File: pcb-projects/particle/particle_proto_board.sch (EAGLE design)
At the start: 5 parts, among them IC1 ATTINY20-SOIC-14S1, IC2 DMC2400UV-SOT563, IC3 DMC2400UV-SOT563

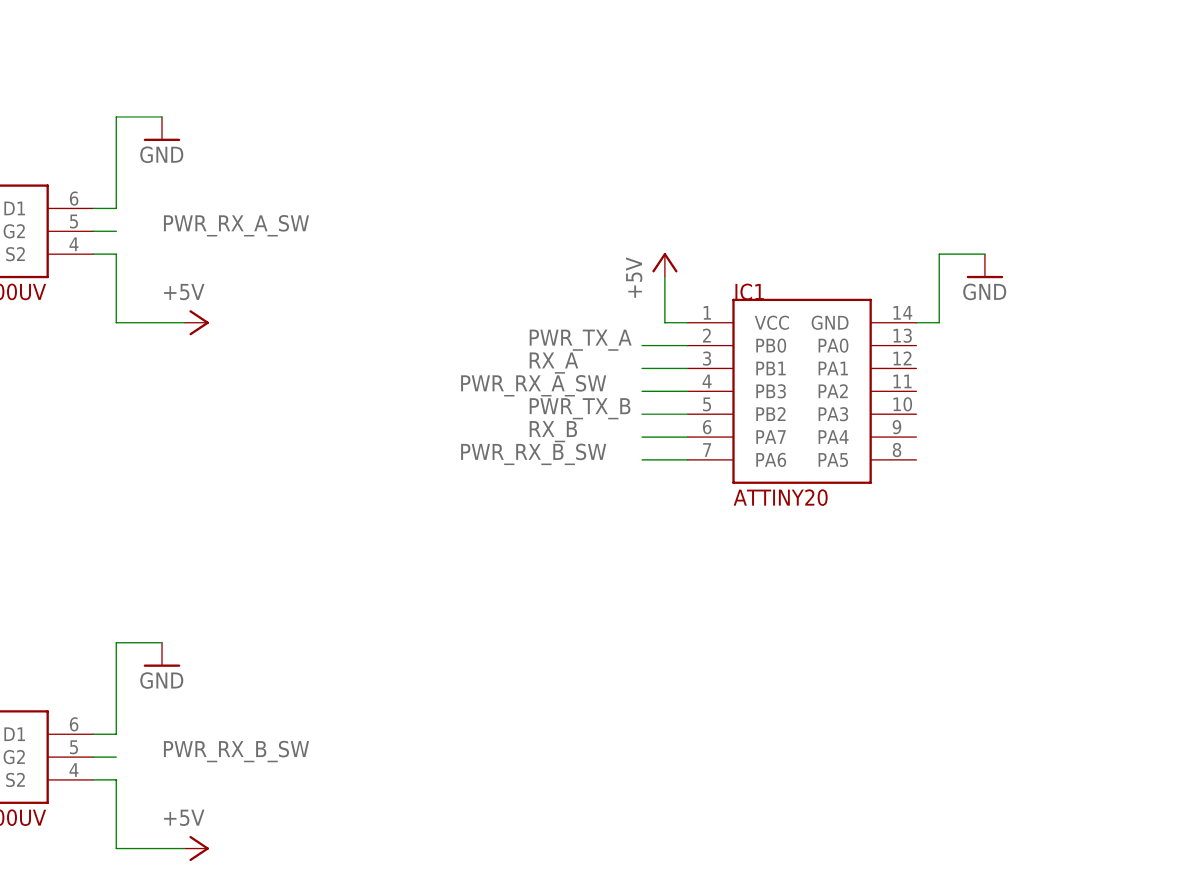
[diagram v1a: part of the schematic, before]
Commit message: begun with tpi connector
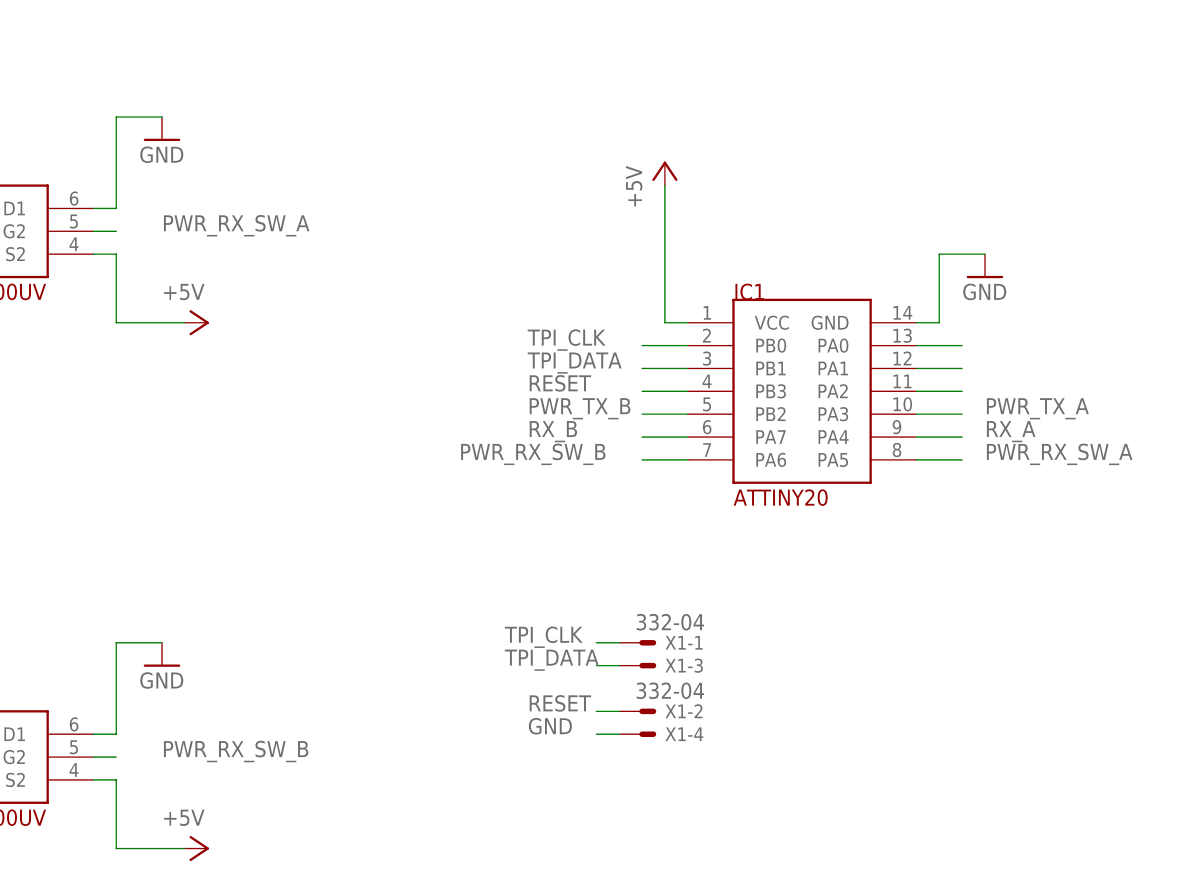
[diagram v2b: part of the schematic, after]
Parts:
- added X1: 332-04, con-garry:332-04
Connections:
- net PWR_RX_B_SW renamed PWR_RX_SW_B
- removed net PWR_RX_A_SW: IC1.PB3, IC2.G2
- new net N$4: IC1.PA2
- new net N$5: IC1.PA1
- new net N$6: IC1.PA0
- new net PWR_RX_SW_A: IC1.PA5, IC2.G2
- new net RESET: IC1.PB3, X1-2.S
- new net TPI_CLK: IC1.PB0, X1-1.S
- new net TPI_DATA: IC1.PB1, X1-3.S
- net GND: now also X1-4.S
- net PWR_TX_A: now also IC1.PA3; no longer IC1.PB0
- net RX_A: now also IC1.PA4; no longer IC1.PB1
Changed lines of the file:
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@@
 <?xml version="1.0" encoding="utf-8"?>
 <!DOCTYPE eagle SYSTEM "eagle.dtd">
-<eagle version="6.6.0">
+<eagle version="7.2.0">
 <drawing>
 <settings>
@@
 <part name="R1" library="rcl" deviceset="R-EU_" device="R1206" value="1k"/>
 <part name="R2" library="rcl" deviceset="R-EU_" device="R1206" value="1k"/>
+<part name="X1" library="con-garry" deviceset="332-04" device=""/>
 </parts>
 <sheets>
@@
 <instance part="IC1" gate="G$1" x="91.44" y="83.82"/>
 <instance part="IC2" gate="G$1" x="0" y="101.6"/>
-<instance part="P+2" gate="1" x="76.2" y="99.06"/>
+<instance part="P+2" gate="1" x="76.2" y="109.22"/>
 <instance part="GND1" gate="1" x="111.76" y="96.52"/>
 <instance part="GND2" gate="1" x="20.32" y="111.76"/>
@@
 <instance part="R1" gate="G$1" x="-22.86" y="114.3" rot="R90"/>
 <instance part="R2" gate="G$1" x="-22.86" y="55.88" rot="R90"/>
+<instance part="X1" gate="-1" x="73.66" y="55.88"/>
+<instance part="X1" gate="-2" x="73.66" y="48.26"/>
+<instance part="X1" gate="-3" x="73.66" y="53.34"/>
+<instance part="X1" gate="-4" x="73.66" y="45.72"/>
 </instances>
 <busses>
@@
 <pinref part="IC1" gate="G$1" pin="VCC"/>
 <wire x1="78.74" y1="91.44" x2="76.2" y2="91.44" width="0.1524" layer="91"/>
-<wire x1="76.2" y1="91.44" x2="76.2" y2="96.52" width="0.1524" layer="91"/>
+<wire x1="76.2" y1="91.44" x2="76.2" y2="106.68" width="0.1524" layer="91"/>
 <pinref part="P+2" gate="1" pin="+5V"/>
 </segment>
@@
 <wire x1="15.24" y1="55.88" x2="20.32" y2="55.88" width="0.1524" layer="91"/>
 </segment>
-</net>
-<net name="PWR_TX_A" class="0">
+<segment>
+<pinref part="X1" gate="-4" pin="S"/>
+<wire x1="71.12" y1="45.72" x2="68.58" y2="45.72" width="0.1524" layer="91"/>
+<label x="60.96" y="45.72" size="1.778" layer="95"/>
+</segment>
+</net>
+<net name="TPI_CLK" class="0">
 <segment>
 <pinref part="IC1" gate="G$1" pin="PB0"/>
@@
 </segment>
 <segment>
-<pinref part="IC2" gate="G$1" pin="G1"/>
-<wire x1="-12.7" y1="101.6" x2="-15.24" y2="101.6" width="0.1524" layer="91"/>
-<label x="-30.48" y="101.6" size="1.778" layer="95"/>
+<pinref part="X1" gate="-1" pin="S"/>
+<wire x1="71.12" y1="55.88" x2="68.58" y2="55.88" width="0.1524" layer="91"/>
+<label x="58.42" y="55.88" size="1.778" layer="95"/>
 </segment>
 </net>
@@
 </segment>
 </net>
-<net name="RX_A" class="0">
+<net name="TPI_DATA" class="0">
 <segment>
 <pinref part="IC1" gate="G$1" pin="PB1"/>
@@
 </segment>
 <segment>
-<pinref part="IC2" gate="G$1" pin="D2"/>
-<wire x1="-12.7" y1="99.06" x2="-15.24" y2="99.06" width="0.1524" layer="91"/>
-<label x="-30.48" y="99.06" size="1.778" layer="95"/>
-</segment>
-</net>
-<net name="PWR_RX_A_SW" class="0">
+<pinref part="X1" gate="-3" pin="S"/>
+<wire x1="71.12" y1="53.34" x2="68.58" y2="53.34" width="0.1524" layer="91"/>
+<label x="58.42" y="53.34" size="1.778" layer="95"/>
+</segment>
+</net>
+<net name="RESET" class="0">
 <segment>
 <pinref part="IC1" gate="G$1" pin="PB3"/>
 <wire x1="78.74" y1="83.82" x2="73.66" y2="83.82" width="0.1524" layer="91"/>
-<label x="53.34" y="83.82" size="1.778" layer="95"/>
-</segment>
-<segment>
-<pinref part="IC2" gate="G$1" pin="G2"/>
-<wire x1="12.7" y1="101.6" x2="15.24" y2="101.6" width="0.1524" layer="91"/>
-<label x="20.32" y="101.6" size="1.778" layer="95"/>
+<label x="60.96" y="83.82" size="1.778" layer="95"/>
+</segment>
+<segment>
+<pinref part="X1" gate="-2" pin="S"/>
+<wire x1="71.12" y1="48.26" x2="68.58" y2="48.26" width="0.1524" layer="91"/>
+<label x="60.96" y="48.26" size="1.778" layer="95"/>
 </segment>
 </net>
@@
 </segment>
 </net>
-<net name="PWR_RX_B_SW" class="0">
+<net name="PWR_RX_SW_B" class="0">
 <segment>
 <pinref part="IC1" gate="G$1" pin="PA6"/>
@@
 </segment>
 </net>
+<net name="PWR_RX_SW_A" class="0">
+<segment>
+<pinref part="IC1" gate="G$1" pin="PA5"/>
+<wire x1="104.14" y1="76.2" x2="109.22" y2="76.2" width="0.1524" layer="91"/>
+<label x="111.76" y="76.2" size="1.778" layer="95"/>
+</segment>
+<segment>
+<pinref part="IC2" gate="G$1" pin="G2"/>
+<wire x1="12.7" y1="101.6" x2="15.24" y2="101.6" width="0.1524" layer="91"/>
+<label x="20.32" y="101.6" size="1.778" layer="95"/>
+</segment>
+</net>
+<net name="RX_A" class="0">
+<segment>
+<pinref part="IC1" gate="G$1" pin="PA4"/>
+<wire x1="104.14" y1="78.74" x2="109.22" y2="78.74" width="0.1524" layer="91"/>
+<label x="111.76" y="78.74" size="1.778" layer="95"/>
+</segment>
+<segment>
+<pinref part="IC2" gate="G$1" pin="D2"/>
+<wire x1="-12.7" y1="99.06" x2="-15.24" y2="99.06" width="0.1524" layer="91"/>
+<label x="-30.48" y="99.06" size="1.778" layer="95"/>
+</segment>
+</net>
+<net name="PWR_TX_A" class="0">
+<segment>
+<pinref part="IC1" gate="G$1" pin="PA3"/>
+<wire x1="104.14" y1="81.28" x2="109.22" y2="81.28" width="0.1524" layer="91"/>
+<label x="111.76" y="81.28" size="1.778" layer="95"/>
+</segment>
+<segment>
+<pinref part="IC2" gate="G$1" pin="G1"/>
+<wire x1="-12.7" y1="101.6" x2="-15.24" y2="101.6" width="0.1524" layer="91"/>
+<label x="-30.48" y="101.6" size="1.778" layer="95"/>
+</segment>
+</net>
+<net name="N$4" class="0">
+<segment>
+<pinref part="IC1" gate="G$1" pin="PA2"/>
+<wire x1="104.14" y1="83.82" x2="109.22" y2="83.82" width="0.1524" layer="91"/>
+</segment>
+</net>
+<net name="N$5" class="0">
+<segment>
+<pinref part="IC1" gate="G$1" pin="PA1"/>
+<wire x1="104.14" y1="86.36" x2="109.22" y2="86.36" width="0.1524" layer="91"/>
+</segment>
+</net>
+<net name="N$6" class="0">
+<segment>
+<pinref part="IC1" gate="G$1" pin="PA0"/>
+<wire x1="104.14" y1="88.9" x2="109.22" y2="88.9" width="0.1524" layer="91"/>
+</segment>
+</net>

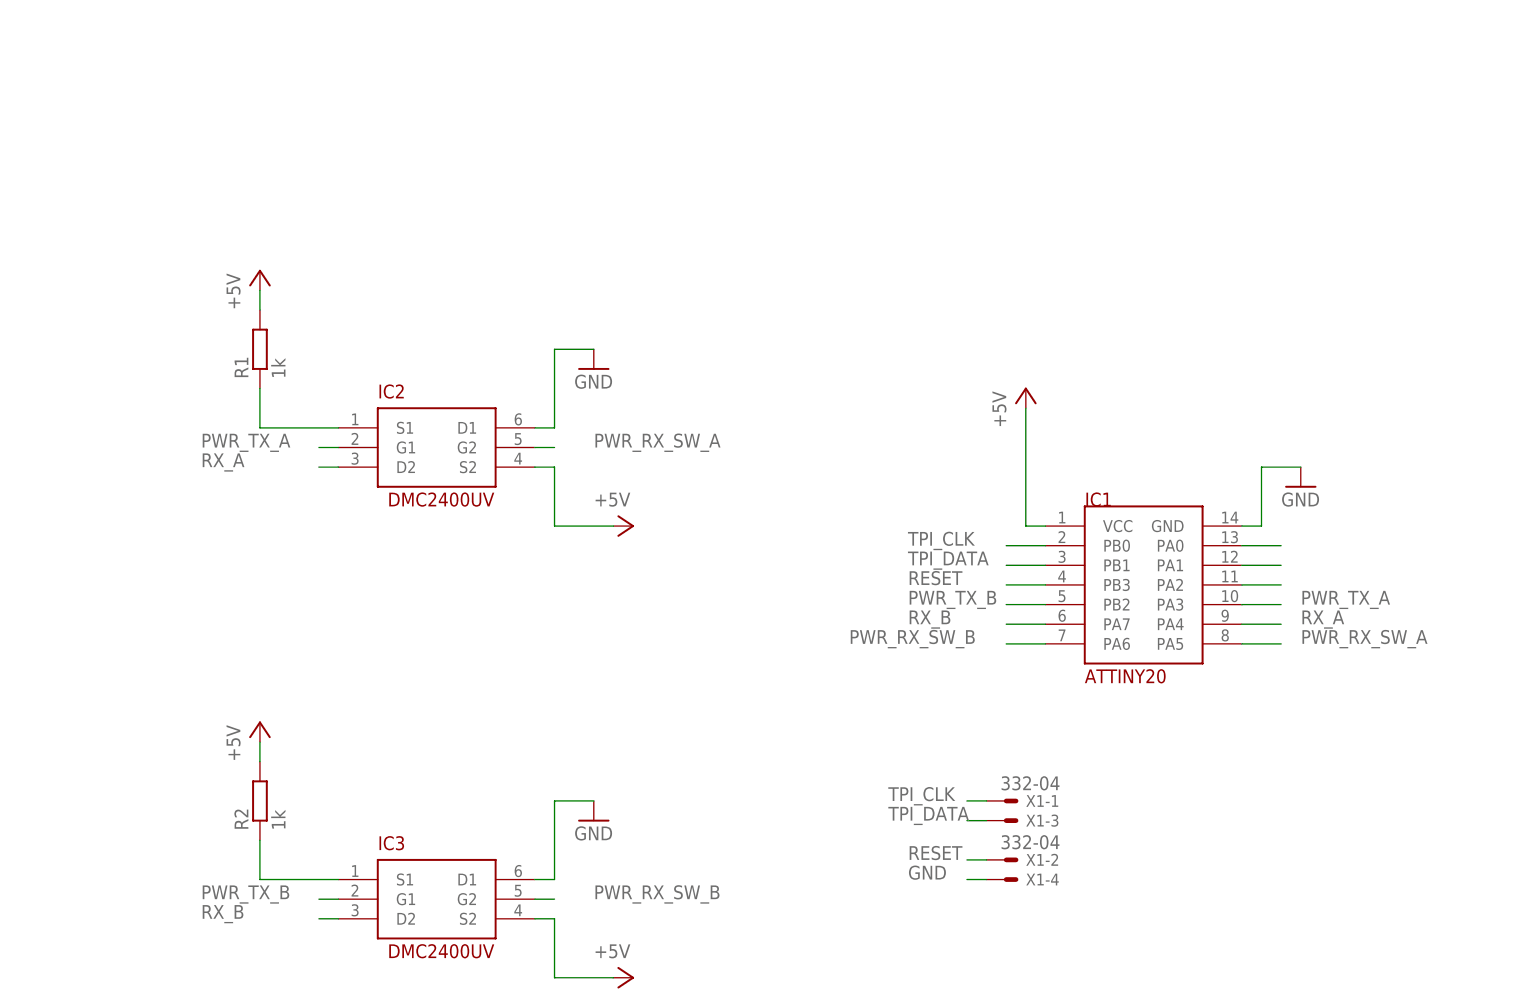
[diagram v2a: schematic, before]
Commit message: begun with routing
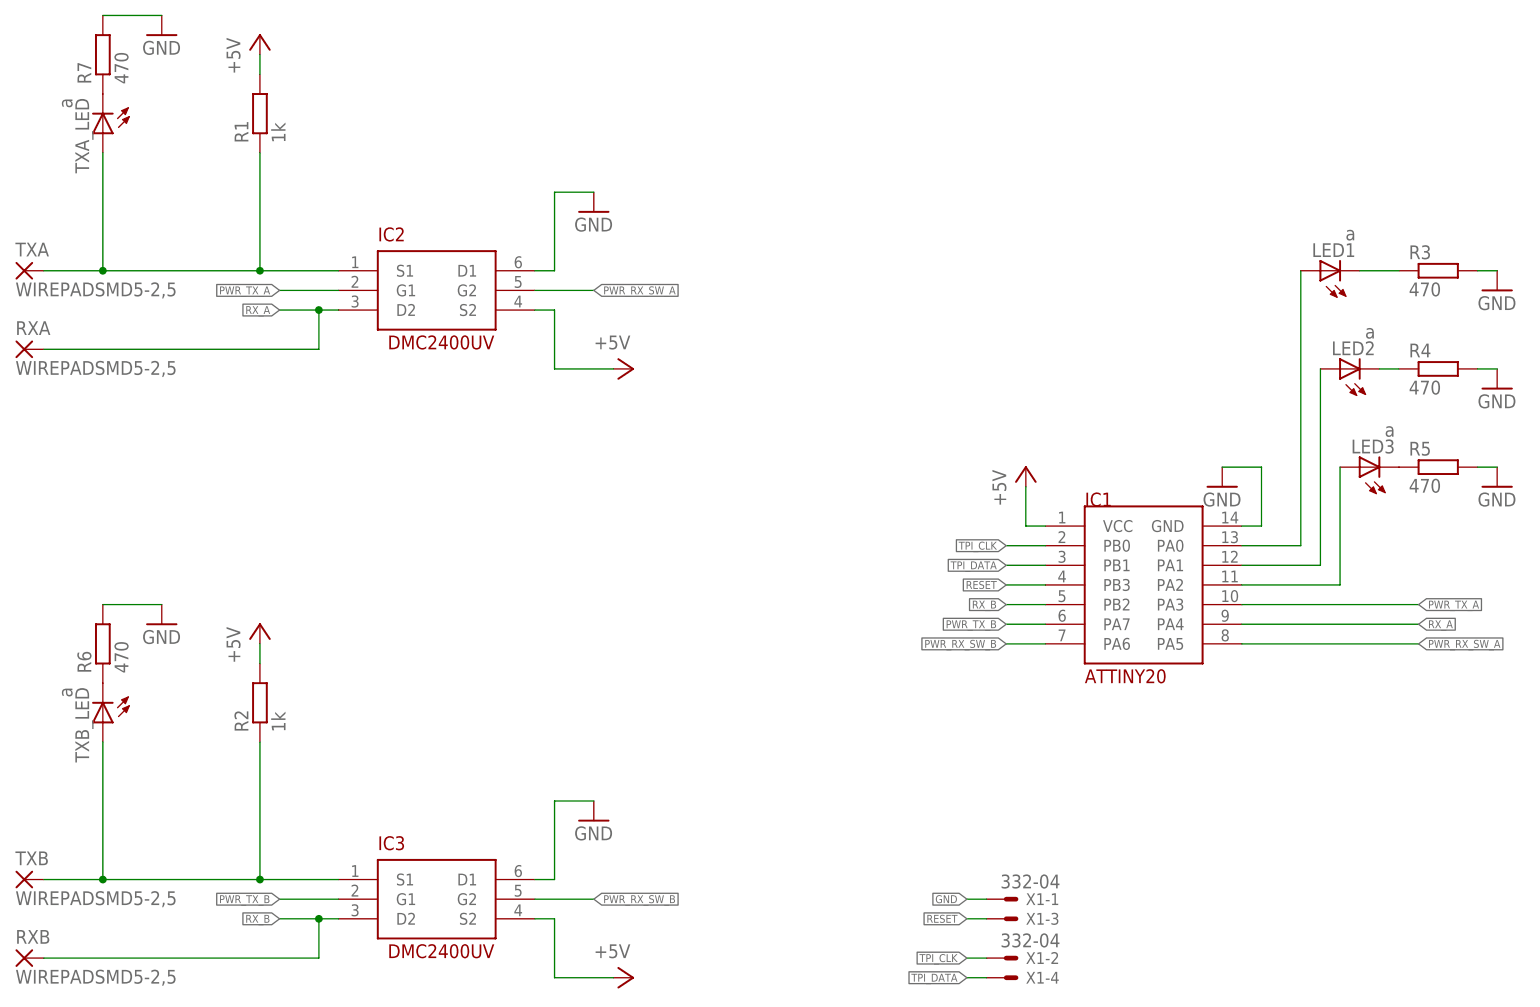
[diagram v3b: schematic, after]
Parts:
- added LED1, LED2, LED3, TXA_LED, TXB_LED: a, led:LEDKA-3528ASYC
- added R3, R4, R5, R6, R7: 470, rcl:R-EU_R1206
- added RXA, RXB, TXA, TXB: WIREPADSMD5-2,5, wirepad:WIREPADSMD5-2,5
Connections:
- removed net PWR_TX_A_A_A1: IC3.S1, R2.1
- new net N$1: IC1.PA0, LED1.A
- new net N$2: IC1.PA2, LED3.A
- new net N$3: IC1.PA1, LED2.A
- new net N$7: R7.1, TXA_LED.C
- new net N$8: LED3.C, R5.1
- new net TXB: IC3.S1, R2.1, TXB.P, TXB_LED.A
- net GND: now also R3.2, R4.2, R5.2, R6.2, R7.2, X1-1.S; no longer X1-4.S
- net N$4: now also LED1.C, R3.1; no longer IC1.PA2
- net N$5: now also R6.1, TXB_LED.C; no longer IC1.PA1
- net N$6: now also LED2.C, R4.1; no longer IC1.PA0
- net PWR_TX_A_A_A: now also TXA.P, TXA_LED.A
- net PWR_TX_B: now also IC1.PA7; no longer IC1.PB2
- net RESET: now also X1-3.S; no longer X1-2.S
- net RX_A: now also RXA.P
- net RX_B: now also IC1.PB2, RXB.P; no longer IC1.PA7
- net TPI_CLK: now also X1-2.S; no longer X1-1.S
- net TPI_DATA: now also X1-4.S; no longer X1-3.S
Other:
- moved on the sheet: IC2, R1, R2, X1-1, X1-2, X1-3, X1-4
